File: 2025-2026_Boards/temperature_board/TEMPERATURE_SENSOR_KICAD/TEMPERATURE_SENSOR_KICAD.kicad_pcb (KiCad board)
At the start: 2 copper layers, 73.3 x 75.8 mm, 85 parts, among them J1 LCD Connector Pinout, J10 Conn_01x02_Pin, J11 Conn_01x02_Pin, J12 Conn_01x02_Pin, J13 Conn_01x02_Pin, J14 Conn_01x02_Pin, J15 Conn_01x02_Pin, J16 Conn_01x02_Pin, J17 Conn_01x02_Pin, J18 Conn_01x02_Pin, J19 Conn_01x02_Pin, J2 Conn_01x02_Pin, J20 Conn_01x02_Pin, J21 Conn_01x02_Pin, J22 Conn_01x02_Pin, J23 Conn_01x02_Pin, J24 Conn_01x03_Socket, J25 Conn_01x03_Socket, J3 Conn_01x02_Pin, J4 Conn_01x02_Pin, J5 Conn_01x02_Pin, J6 Conn_01x02_Pin, J7 Conn_01x02_Pin, J8 Conn_01x02_Pin, J9 Conn_01x02_Pin, U1 STM32G431CBT6, U2 TMP235A4DBZR, U3 AMS1117-3.3, U4 TCAN1057AEV-Q1, U5 TPS62932DRLR, U8 AMS1117

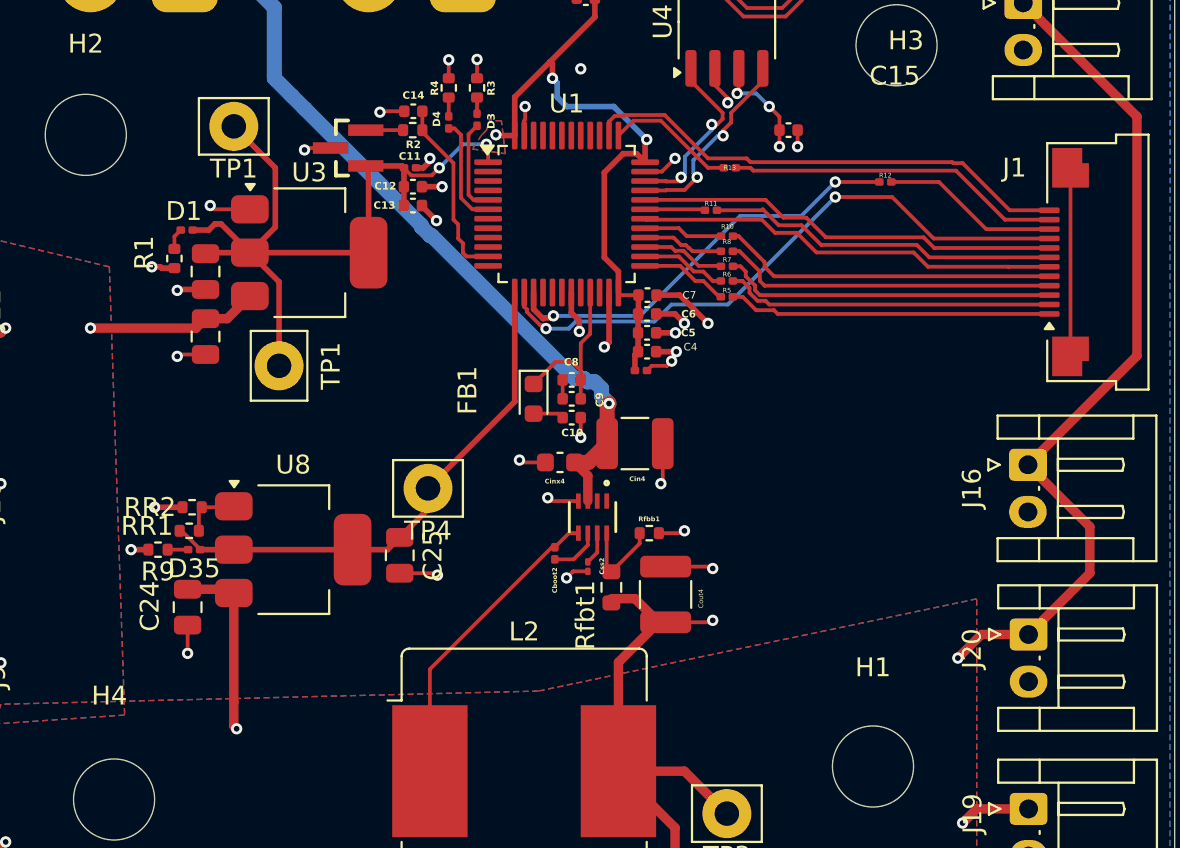
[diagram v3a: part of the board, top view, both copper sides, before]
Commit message: redid led display. can i delete the 2.2v regulator?
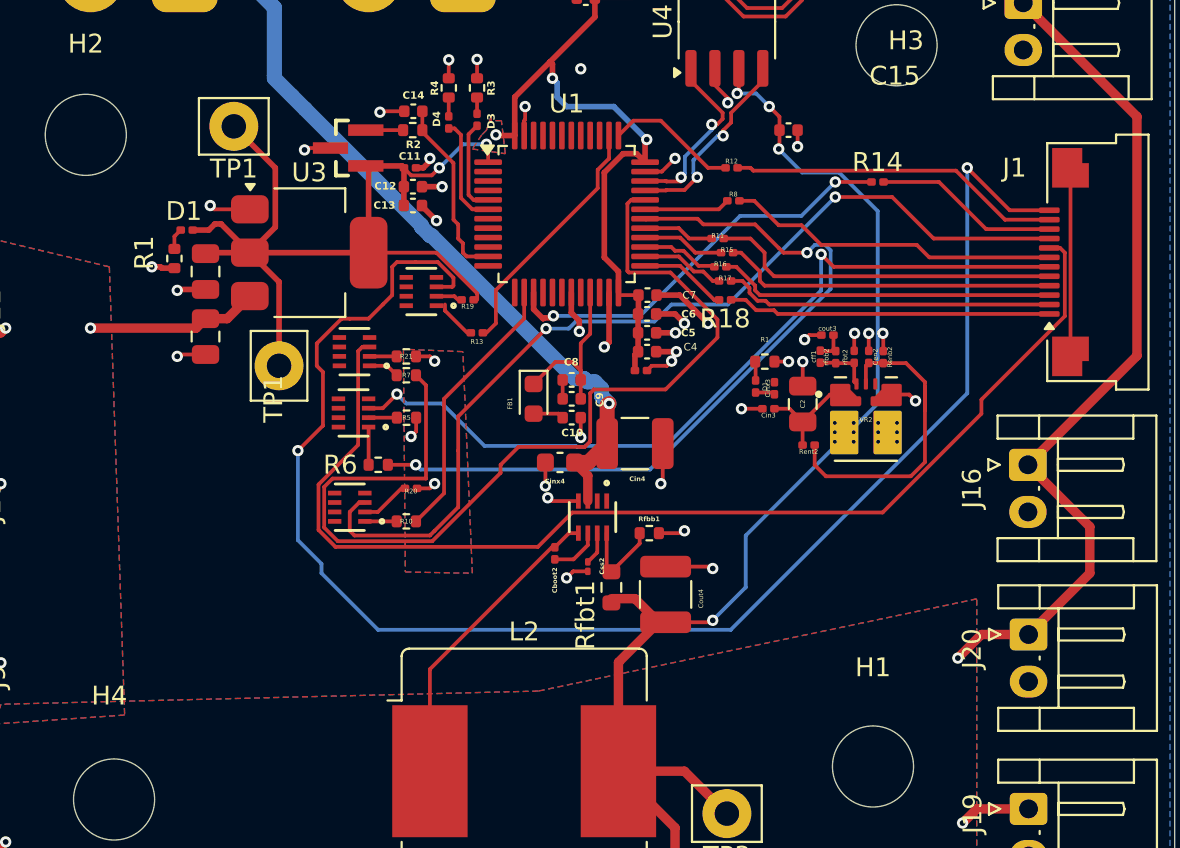
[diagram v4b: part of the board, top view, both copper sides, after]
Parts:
- removed C24, C25: 22u, Capacitor_SMD:C_0805_2012Metric
- removed D35: LED, Capacitor_SMD:C_0201_0603Metric
- removed R9: 1k5, Resistor_SMD:R_0402_1005Metric
- removed RR1: 130, Resistor_SMD:R_0402_1005Metric
- removed RR2: 100, Resistor_SMD:R_0402_1005Metric
- removed TP4: TestPoint, Connector_Pin:Pin_D1.3mm_L10.0mm_W3.5mm_Flat
- removed U8: AMS1117, Package_TO_SOT_SMD:SOT-223-3_TabPin2
- added C2: 22u, Capacitor_SMD:C_0805_2012Metric, F.Cu at (125.3, 134.0)
- added Cen2: 10n, Capacitor_SMD:C_0201_0603Metric, F.Cu at (128.8, 131.5)
- added Cin3: 10u, Capacitor_SMD:C_0201_0603Metric, F.Cu at (123.5, 134.3)
- added Cinx3: 100n, Capacitor_SMD:C_0201_0603Metric, F.Cu at (123.8, 133.2)
- added D1: LED, Capacitor_SMD:C_0201_0603Metric, F.Cu at (122.8, 133.1)
- added Q1: Q_NPN_BCE, AdditionalFootprintLibrary:SOT8_DRL_TEX, F.Cu at (101.4, 134.5)
- added Q3: Q_NPN_BCE, AdditionalFootprintLibrary:SOT8_DRL_TEX, F.Cu at (101.5, 131.2)
- added Q4: Q_NPN_BCE, AdditionalFootprintLibrary:SOT8_DRL_TEX, F.Cu at (101.2, 139.5)
- added Q5: Q_PNP_BCE, AdditionalFootprintLibrary:SOT8_DRL_TEX, F.Cu at (105.0, 128.1)
- added R1: 1k5, Resistor_SMD:R_0402_1005Metric, F.Cu at (123.3, 131.8)
- added R14: 80, Resistor_SMD:R_0201_0603Metric, F.Cu at (129.2, 122.2)
- added R15: 80, Resistor_SMD:R_0201_0603Metric, F.Cu at (121.3, 126.0)
- added R16: 80, Resistor_SMD:R_0201_0603Metric, F.Cu at (120.9, 126.8)
- added R17: 80, Resistor_SMD:R_0201_0603Metric, F.Cu at (121.2, 127.5)
- added R18: 80, Resistor_SMD:R_0201_0603Metric, F.Cu at (121.2, 128.5)
- added R19: 55, Resistor_SMD:R_0201_0603Metric, F.Cu at (107.5, 128.5)
- added R20: 55, Resistor_SMD:R_0201_0603Metric, F.Cu at (104.5, 138.5)
- added R21: 55, Resistor_SMD:R_0402_1005Metric, F.Cu at (104.2, 131.5)
- added Renb2: 10k, Resistor_SMD:R_0201_0603Metric, F.Cu at (129.5, 131.5)
- added Rent2: 10k, Resistor_SMD:R_0201_0603Metric, F.Cu at (125.6, 136.2)
- added VR2: TPSM863252RDXR, AdditionalFootprintLibrary:VREG_TPSM863252RDXR, F.Cu at (128.6, 134.9)
- added cff1: 22p, Capacitor_SMD:C_0201_0603Metric, F.Cu at (126.2, 131.5)
- added cout3: 22p, Capacitor_SMD:C_0201_0603Metric, F.Cu at (126.6, 130.4)
- added rfbb2: 30k, Resistor_SMD:R_0201_0603Metric, F.Cu at (128.0, 131.5)
- added rfbt2: 80.6k, Resistor_SMD:R_0201_0603Metric, F.Cu at (127.0, 131.5)
- R10, R6, R7: value 100 -> 10k; footprint Resistor_SMD:R_0201_0603Metric -> Resistor_SMD:R_0402_1005Metric
- R11, R12, R8: value 100 -> 80
- R13: value 100 -> 10k
- R5: value 100 -> 55; footprint Resistor_SMD:R_0201_0603Metric -> Resistor_SMD:R_0402_1005Metric
- moved R10 22.8 mm to (104.2, 140.2), turned to 180 degrees
- moved R6 20.9 mm to (102.8, 137.2), turned to 180 degrees
- moved R5 18.2 mm to (104.3, 134.7), turned to 180 degrees
- moved R7 18.0 mm to (104.2, 132.5), turned to 180 degrees
- moved R13 16.0 mm to (108.0, 130.2), turned to 180 degrees
- moved R12 8.19 mm to (121.5, 121.5)
- moved R8 2.69 mm to (121.6, 123.2)
- moved R11 1.54 mm to (120.8, 125.2)
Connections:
- R10 pad 1: Net-(U1-PB15) -> Net-(U1-PA6)
- R10 pad 2: Net-(J1-Pin_5) -> Net-(Q4-B)
- R11 pad 1: Net-(U1-PA9) -> Net-(U1-PB15)
- R11 pad 2: Net-(J1-Pin_7) -> Net-(J1-Pin_5)
- R12 pad 1: Net-(U1-PA7) -> Net-(U1-PA13)
- R12 pad 2: Net-(J1-Pin_10) -> Net-(J1-Pin_11)
- R13 pad 1: Net-(U1-PA13) -> Net-(U1-PA14)
- R13 pad 2: Net-(J1-Pin_11) -> Net-(Q5-B)
- R5 pad 1: Net-(U1-PB11) -> +3.3V
- R5 pad 2: Net-(J1-Pin_1) -> Net-(Q1-C)
- R6 pad 1: Net-(U1-PB12) -> Net-(U1-PA8)
- R6 pad 2: Net-(J1-Pin_2) -> Net-(Q1-B)
- R7 pad 1: Net-(U1-PB13) -> Net-(U1-PA10)
- R7 pad 2: Net-(J1-Pin_3) -> Net-(Q3-B)
- R8 pad 1: Net-(U1-PB14) -> Net-(U1-PA9)
- R8 pad 2: Net-(J1-Pin_4) -> Net-(J1-Pin_7)
- U1 pad 14: Net-(J1-Pin_9) -> Net-(U1-PA6)
- U1 pad 30: Net-(J1-Pin_6) -> Net-(U1-PA8)
- U1 pad 32: Net-(J1-Pin_8) -> Net-(U1-PA10)
- U1 pad 38: Net-(J1-Pin_12) -> Net-(U1-PA14)
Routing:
- net Net-(J1-Pin_12): track 26.3 -> 82.9 mm, vias 0 -> 2
- net Net-(U1-PA10): track 0.00 -> 52.5 mm
- net Net-(U1-PA8): track 0.00 -> 40.5 mm, vias 0 -> 2
- net Net-(J1-Pin_8): track 22.5 -> 60.8 mm
- net +2.2V: track 27.9 -> 1.73 mm
- net 5V: track 203.4 -> 225.7 mm, vias 21 -> 20
- net Net-(J1-Pin_6): track 22.5 -> 43.2 mm, vias 0 -> 2
- net Net-(VR2-EN): track 0.00 -> 17.5 mm
- net Net-(J1-Pin_9): track 33.0 -> 50.4 mm
- net +3.3V: track 86.8 -> 103.5 mm, vias 5 -> 8
- net Net-(U1-PA6): track 0.00 -> 14.5 mm
- net Net-(U1-PA14): track 0.00 -> 12.9 mm
- net Net-(U8-ADJ): track 3.03 -> 0.00 mm
- net Net-(VR2-FB): track 0.00 -> 2.98 mm
- net Net-(Q4-C): track 0.00 -> 2.46 mm
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
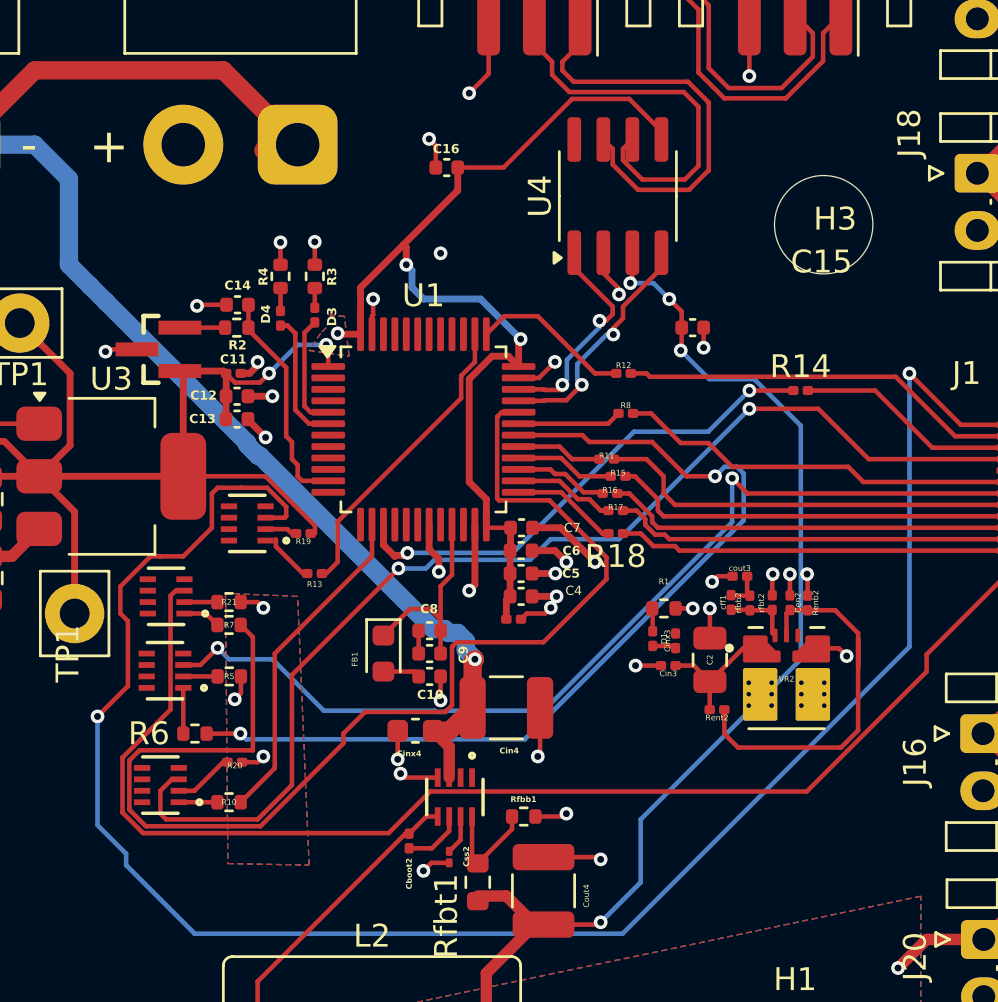
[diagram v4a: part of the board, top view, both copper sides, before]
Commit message: redid led display. can i delete the 2.2v regulator?
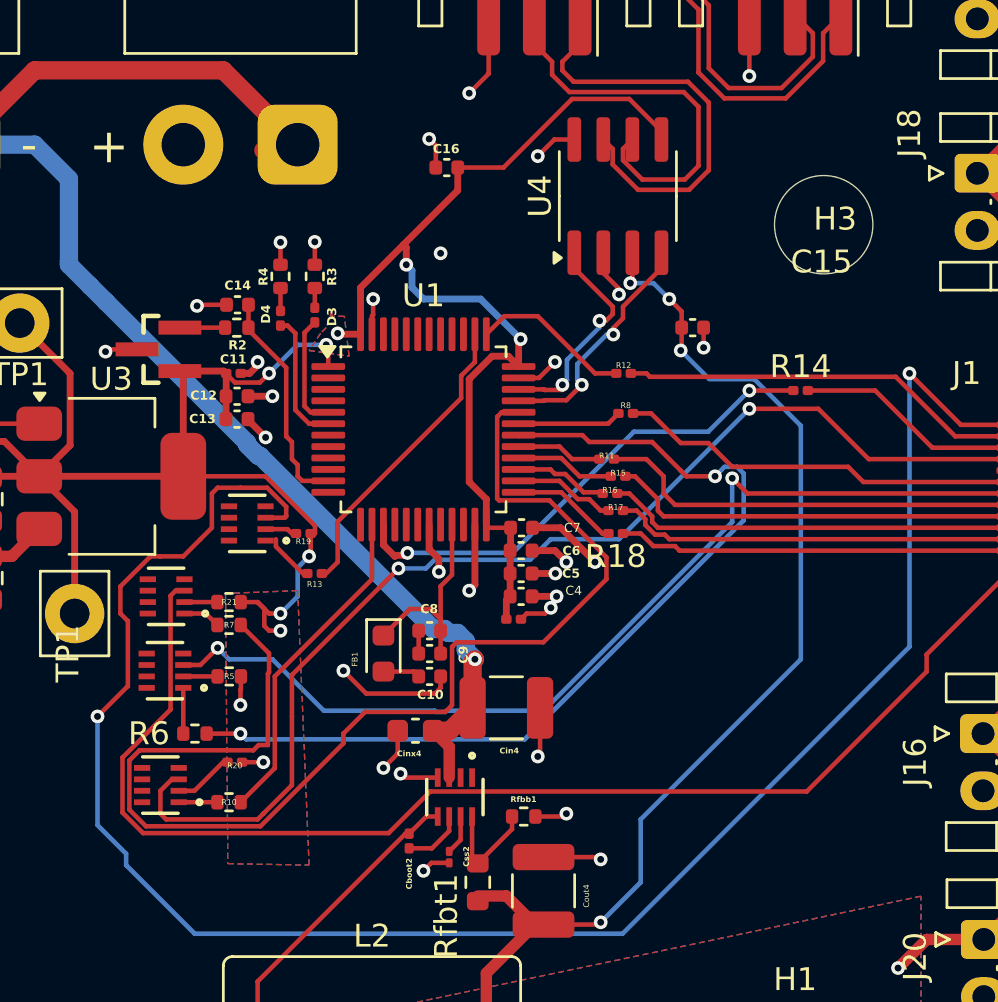
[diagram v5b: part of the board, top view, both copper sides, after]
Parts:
- removed the C2 at (125.3, 134.0)
- removed Cen2: 10n, Capacitor_SMD:C_0201_0603Metric
- removed Cin3: 10u, Capacitor_SMD:C_0201_0603Metric
- removed Cinx3: 100n, Capacitor_SMD:C_0201_0603Metric
- removed the D1 at (122.8, 133.1)
- removed the R1 at (123.3, 131.8)
- removed Renb2, Rent2: 10k, Resistor_SMD:R_0201_0603Metric
- removed VR2: TPSM863252RDXR, AdditionalFootprintLibrary:VREG_TPSM863252RDXR
- removed cff1, cout3: 22p, Capacitor_SMD:C_0201_0603Metric
- removed rfbb2: 30k, Resistor_SMD:R_0201_0603Metric
- removed rfbt2: 80.6k, Resistor_SMD:R_0201_0603Metric
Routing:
- net Net-(VR2-EN): track 17.5 -> 0.00 mm
- net Net-(VR2-FB): track 2.98 -> 0.00 mm
- net +2.2V: track 1.73 -> 0.00 mm
- net GND: track 62.9 -> 61.2 mm, vias 41 -> 34
- net /PWR_LED_K: track 2.15 -> 1.14 mm
- net Net-(U1-PA10): track 52.5 -> 53.4 mm
- net +3.3V: track 103.5 -> 104.2 mm, vias 8 -> 10

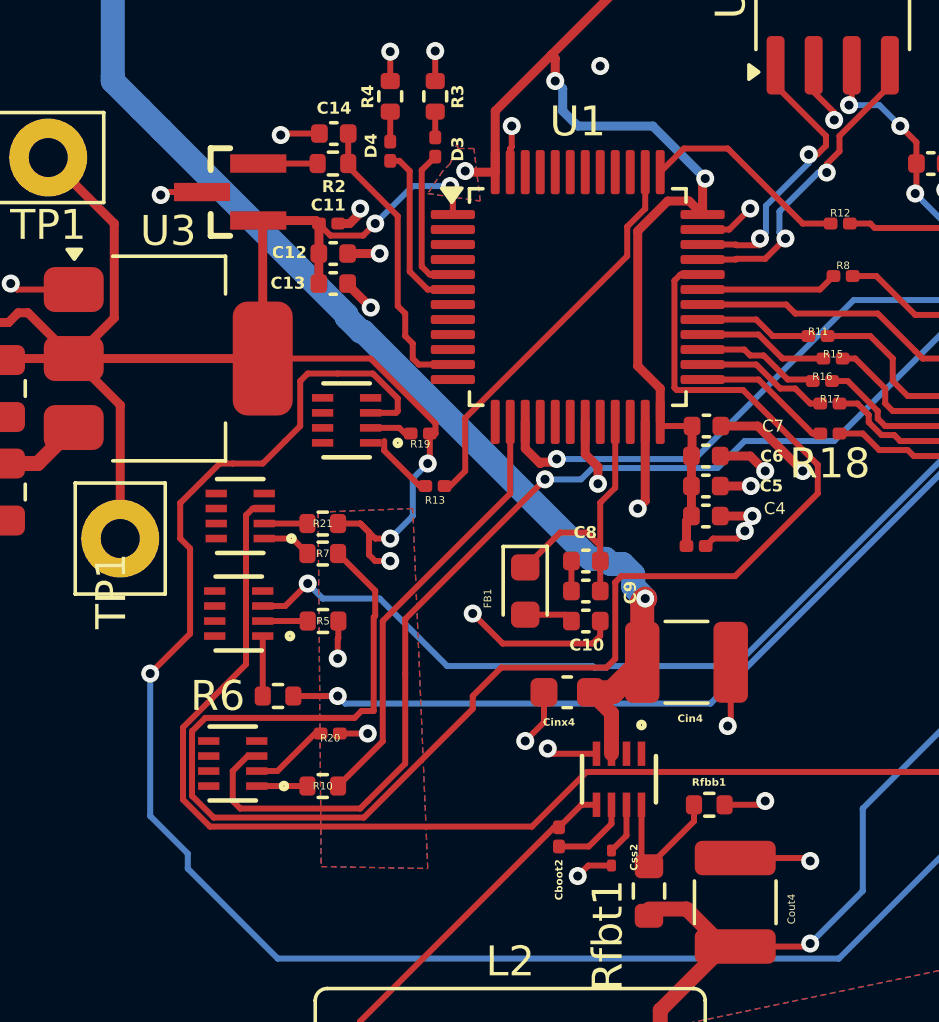
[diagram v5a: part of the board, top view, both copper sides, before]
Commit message: redid led display. can i delete the 2.2v regulator?
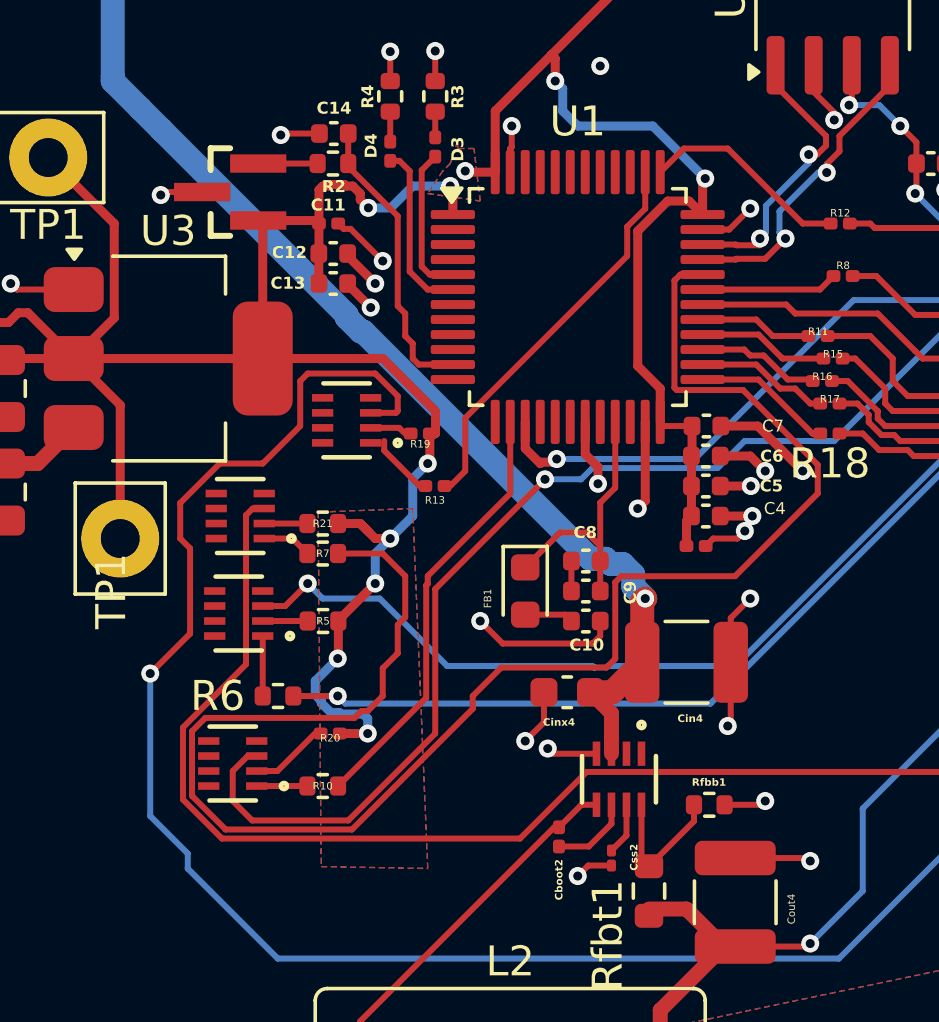
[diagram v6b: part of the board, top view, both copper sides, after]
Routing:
- net +3.3V: track 104.2 -> 111.5 mm
- net GND: track 61.2 -> 64.6 mm, vias 34 -> 35
- net Net-(U1-PA10): track 53.4 -> 55.3 mm

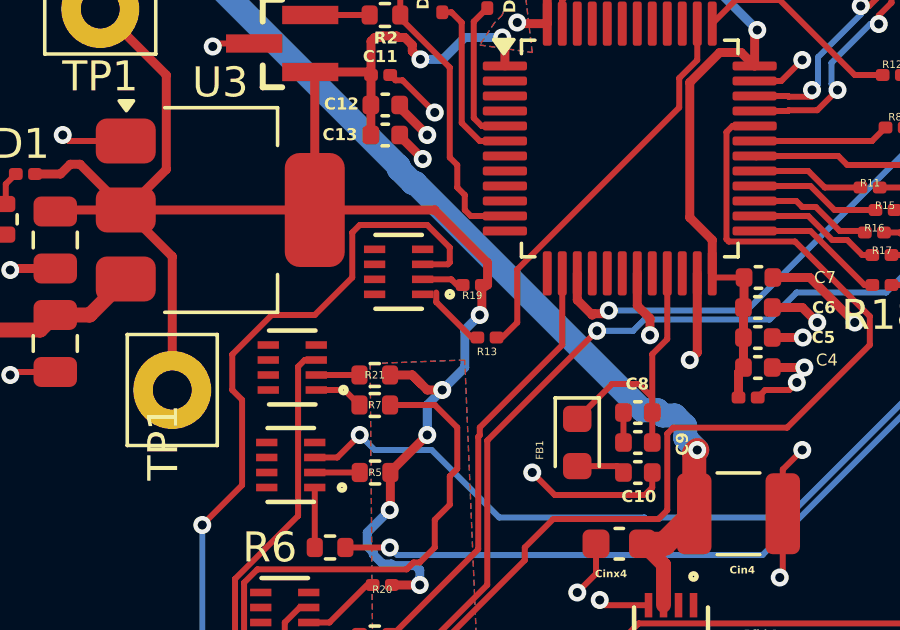
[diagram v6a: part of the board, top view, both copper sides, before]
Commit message: redid led display.
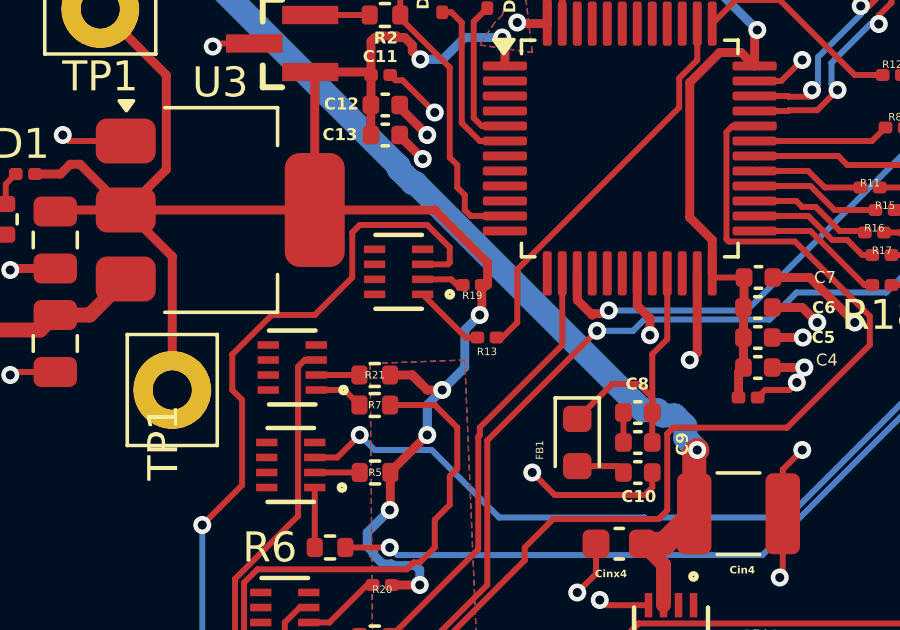
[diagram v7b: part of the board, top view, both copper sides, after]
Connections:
- U1 pad 13: +2.2V -> unconnected-(U1-PA5-Pad13)
